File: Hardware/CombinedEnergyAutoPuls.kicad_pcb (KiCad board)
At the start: 2 copper layers, 174.9 x 67 mm, 131 parts, among them J1 Screw_Terminal_01x04, J101 AudioJack3_Switch, J102 Screw_Terminal_01x03, J103 Conn_3P, J2 Screw_Terminal_01x04, J201 Conn_20P_Female, J202 Conn_20P_Female, J203 Conn_4P_Female, J204 Conn_4P_Female, J205 Barrel_Jack_Switch, J3 Pin_Header_1x6, J4 Arduino_USB-Serial_Card_Conne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, J5 Arduino_USB-Serial_Edge_Conne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, J6 AudioJack3_Switch, J7 Screw_Terminal_01x04, Q1 S8550_PNP, Q101 S8050_NPN, Q2 S8050_NPN, Q3 S8050_NPN, SW201 THT_SW_4_Tactile, U1 L78S05CV, U101 LM358DR2G, U102 78L05, U201 PC817, U202 PC817, U203 PC817, U204 PC817, U205 PC817, U206 PC817, U207 PC817, U208 PC817, U209 PC817, U210 PC817, U211 PC817, U212 L78S05CV

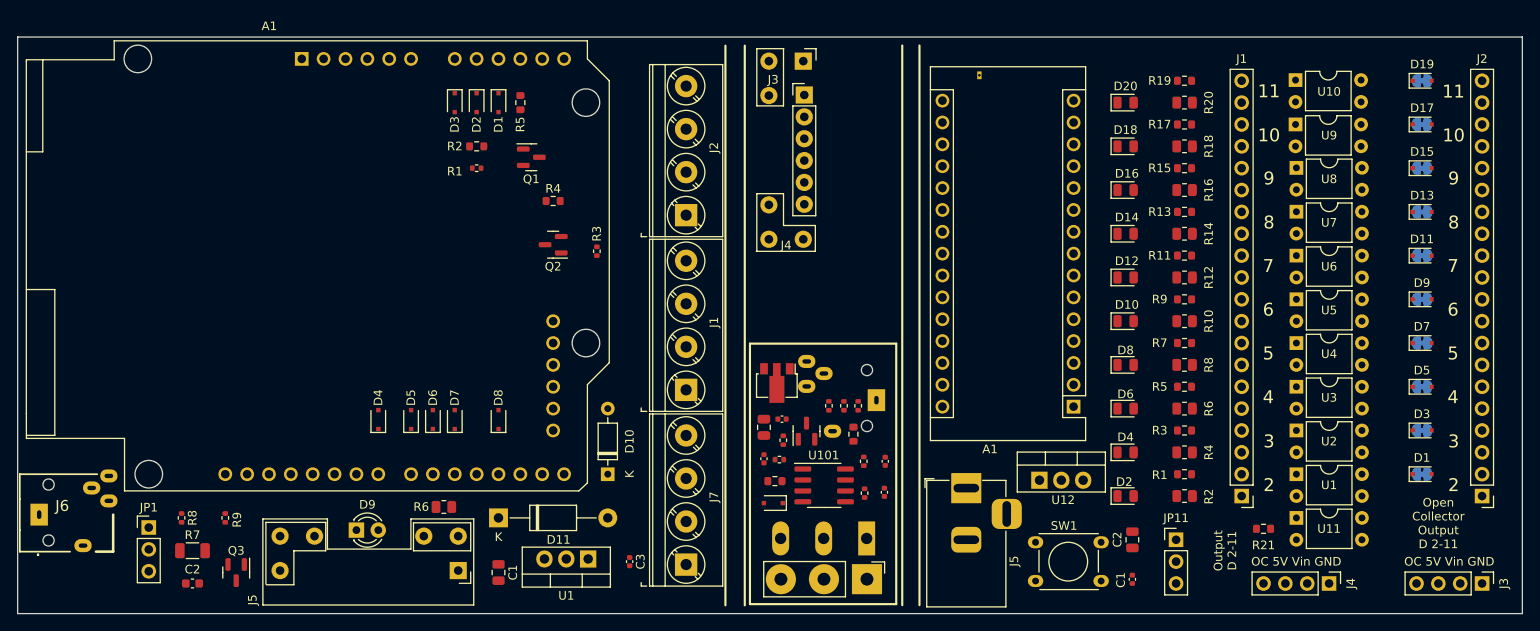
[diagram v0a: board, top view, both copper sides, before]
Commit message: PCB Auto routed.
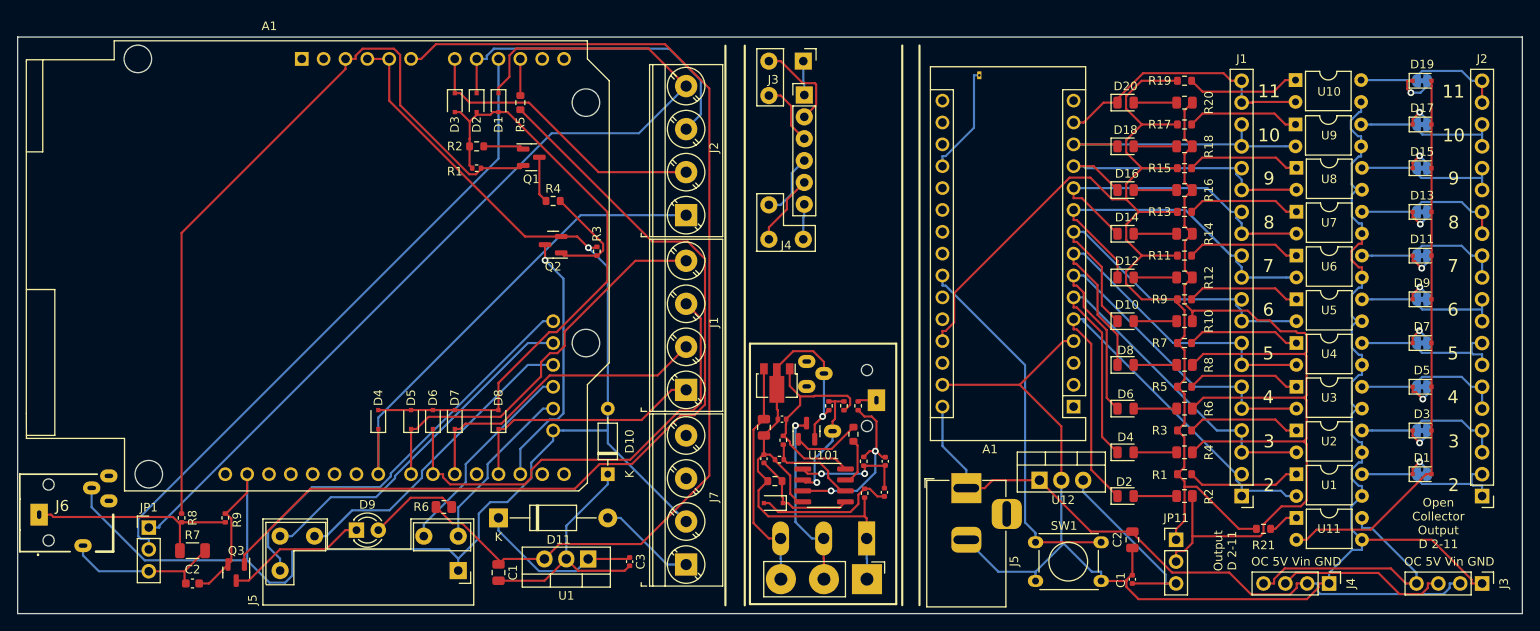
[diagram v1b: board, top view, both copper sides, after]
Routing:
- net GND: track 0.00 -> 182.0 mm, vias 0 -> 1
- net GND4: track 0.00 -> 180.1 mm
- net /Arduino_5V: track 0.00 -> 132.6 mm
- net Net-(JP211-Pad2): track 0.00 -> 128.7 mm
- net Net-(A1-Pad6): track 0.00 -> 121.5 mm
- net Net-(D1-Pad1): track 0.00 -> 111.4 mm
- net Net-(Q3-Pad1): track 0.00 -> 107.5 mm
- net +5V: track 0.00 -> 92.0 mm
- net Vin: track 0.00 -> 76.7 mm
- net Net-(A1-Pad9): track 0.00 -> 75.4 mm
- net Net-(D1-Pad2): track 0.00 -> 72.1 mm
- net GND2: track 0.00 -> 65.9 mm, vias 0 -> 1
- net Net-(D201-Pad2): track 0.00 -> 64.6 mm
- net Net-(A201-Pad5): track 0.00 -> 59.4 mm
- net Net-(A1-Pad21): track 0.00 -> 57.4 mm
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
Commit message: UPD: minor track changes to PCB
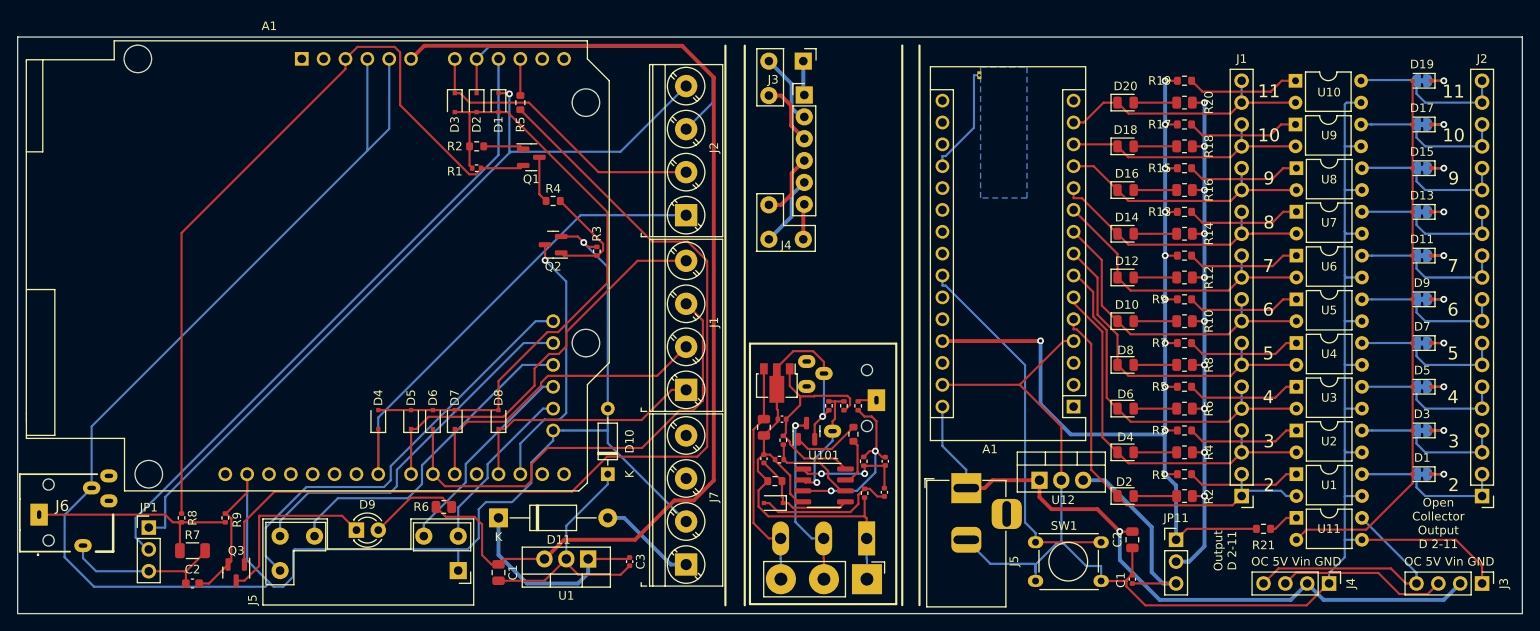
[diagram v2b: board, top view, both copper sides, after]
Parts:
- moved U210 0.08 mm to (148.5, 5.08)
- turned D201 to 180 degrees
- turned D203 to 180 degrees
- turned D205 to 180 degrees
- turned D207 to 180 degrees
- turned D209 to 180 degrees
- turned D211 to 180 degrees
- turned D213 to 180 degrees
- turned D215 to 180 degrees
- turned D217 to 180 degrees
- turned D219 to 180 degrees
- renumbered R½ to R202
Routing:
- net Net-(JP211-Pad2): track 128.7 -> 69.7 mm, vias 0 -> 10
- net GND: track 182.0 -> 236.9 mm
- net /Arduino_5V: track 132.6 -> 112.7 mm, vias 0 -> 11
- net Net-(D1-Pad1): track 111.4 -> 93.9 mm, vias 0 -> 1
- net Net-(A201-Pad5): track 59.4 -> 48.0 mm
- net Net-(A201-Pad6): track 55.2 -> 44.5 mm
- net GND4: track 180.1 -> 190.5 mm
- net Net-(A201-Pad7): track 51.6 -> 42.4 mm
- net Net-(A201-Pad8): track 48.0 -> 39.4 mm
- net Net-(A201-Pad9): track 44.7 -> 37.1 mm
- net Net-(A201-Pad10): track 41.1 -> 34.6 mm
- net Net-(Q3-Pad1): track 107.5 -> 112.9 mm
- net Net-(A201-Pad11): track 37.8 -> 32.4 mm
- net Net-(D9-Pad1): track 16.4 -> 21.2 mm
- net Net-(A201-Pad12): track 35.0 -> 30.6 mm
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- added copper zone on B.Cu, net Net-(A201-Pad19)
